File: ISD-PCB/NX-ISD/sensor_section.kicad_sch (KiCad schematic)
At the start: 19 parts, among them U10 BNO085, U12 OPT3001DNPR, U3 MAX17048G_T10, U4 RV-3028-C7, U5 MAX30102, U6 BME690, Y2 32.768

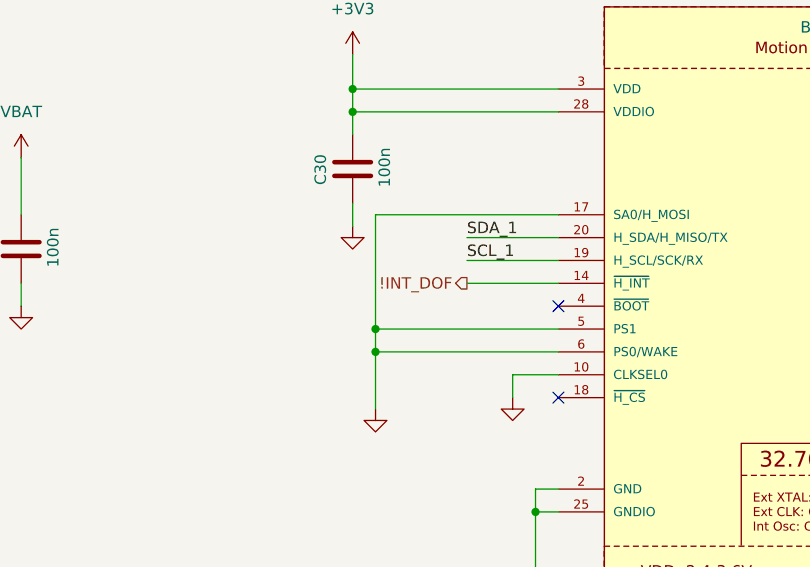
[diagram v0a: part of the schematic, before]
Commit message: Fixed: polarity of NPM Pmos
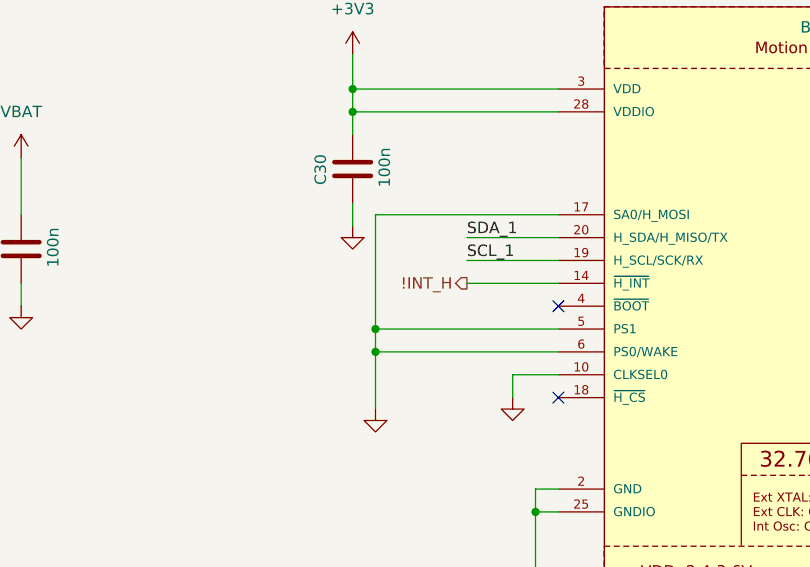
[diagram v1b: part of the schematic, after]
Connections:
- net !INT_DOF renamed !INT_H
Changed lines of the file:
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@@
 		)
 	)
-	(hierarchical_label "!INT_DOF"
+	(hierarchical_label "!INT_H"
 		(shape output)
 		(at 152.4 59.69 180)

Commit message: updated labels
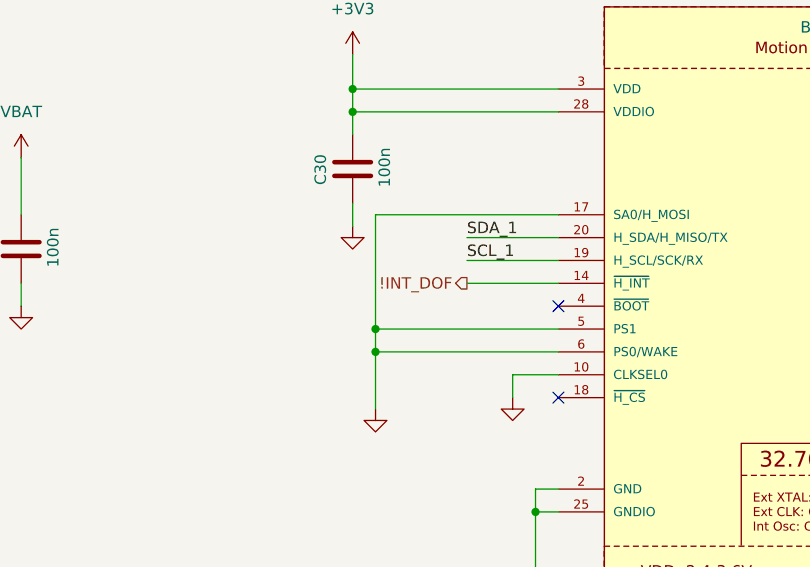
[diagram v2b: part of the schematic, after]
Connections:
- net !INT_H renamed !INT_DOF
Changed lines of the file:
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@@
 		)
 	)
-	(hierarchical_label "!INT_H"
+	(hierarchical_label "!INT_DOF"
 		(shape output)
 		(at 152.4 59.69 180)
